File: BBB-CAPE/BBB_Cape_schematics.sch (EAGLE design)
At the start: 63 parts, among them IC1 EEPROM-I2CSMD

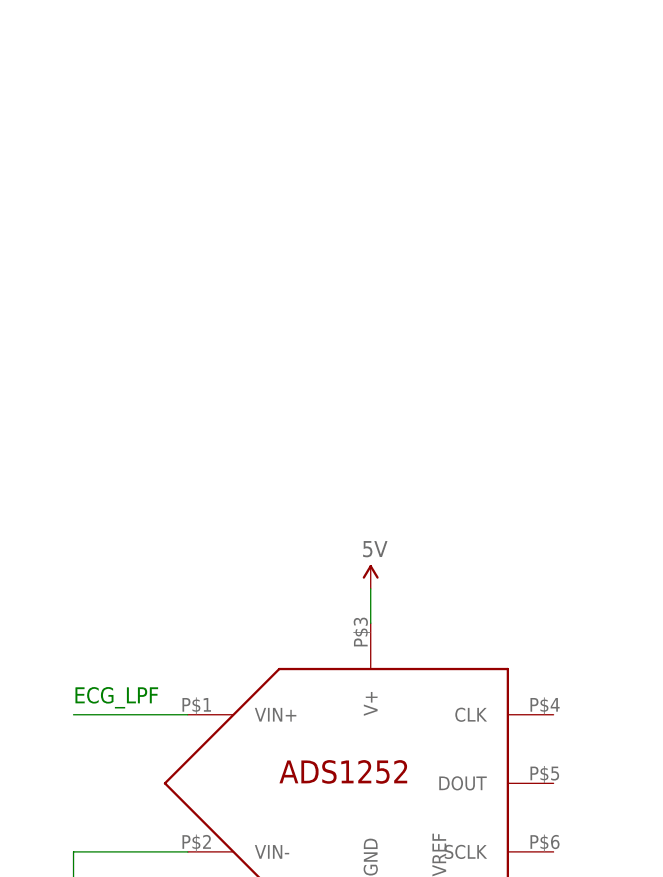
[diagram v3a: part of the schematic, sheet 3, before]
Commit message: Add Clock ATS16ASM-1 to BBB_Cape_schematics.sch
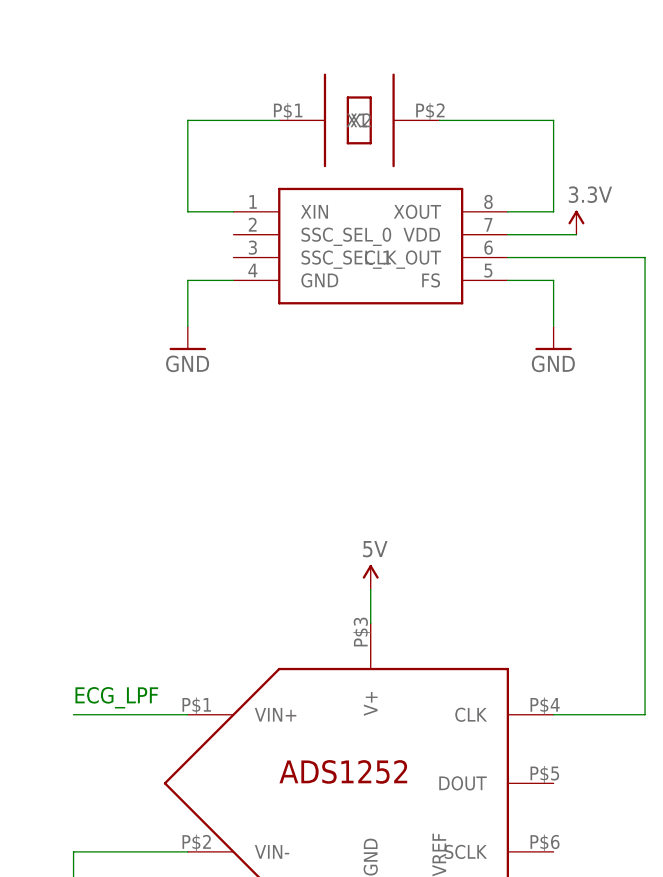
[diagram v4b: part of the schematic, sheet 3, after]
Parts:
- added U$10: CDCS502, Components:CDCS502
- added U$23: ATS16ASM-1, Components:ATS16ASM-1
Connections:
- new net N$27: U$10.XIN, U$23.X1
- new net N$28: U$10.XOUT, U$23.X2
- new net N$29: U$10.CLK_OUT, U$19.CLK
- net 3.3V: now also U$10.VDD
- net GND: now also U$10.FS, U$10.GND

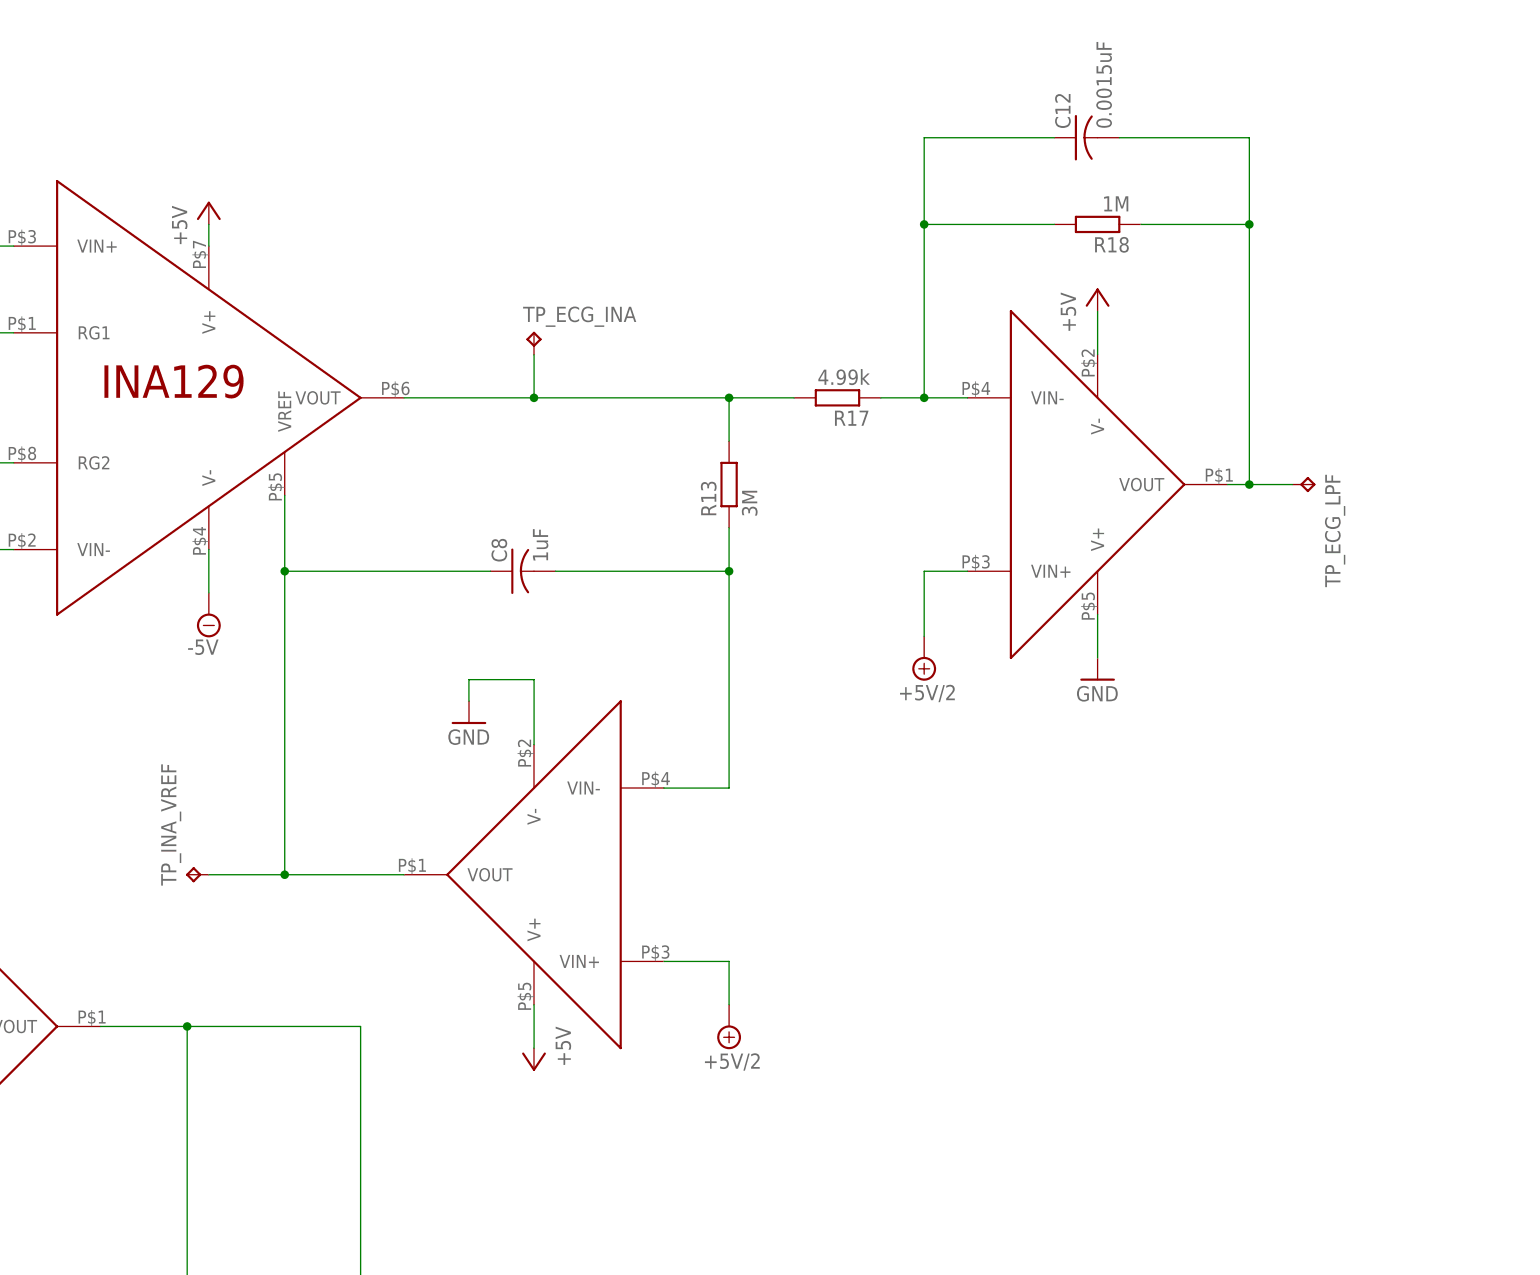
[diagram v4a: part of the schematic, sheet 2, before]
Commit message: Add Resistors to INA129 HPF and LMP2021 LPF for selecting different cut-off frequency; Add DIP Switch  in BBB_Cape_schematics.sch
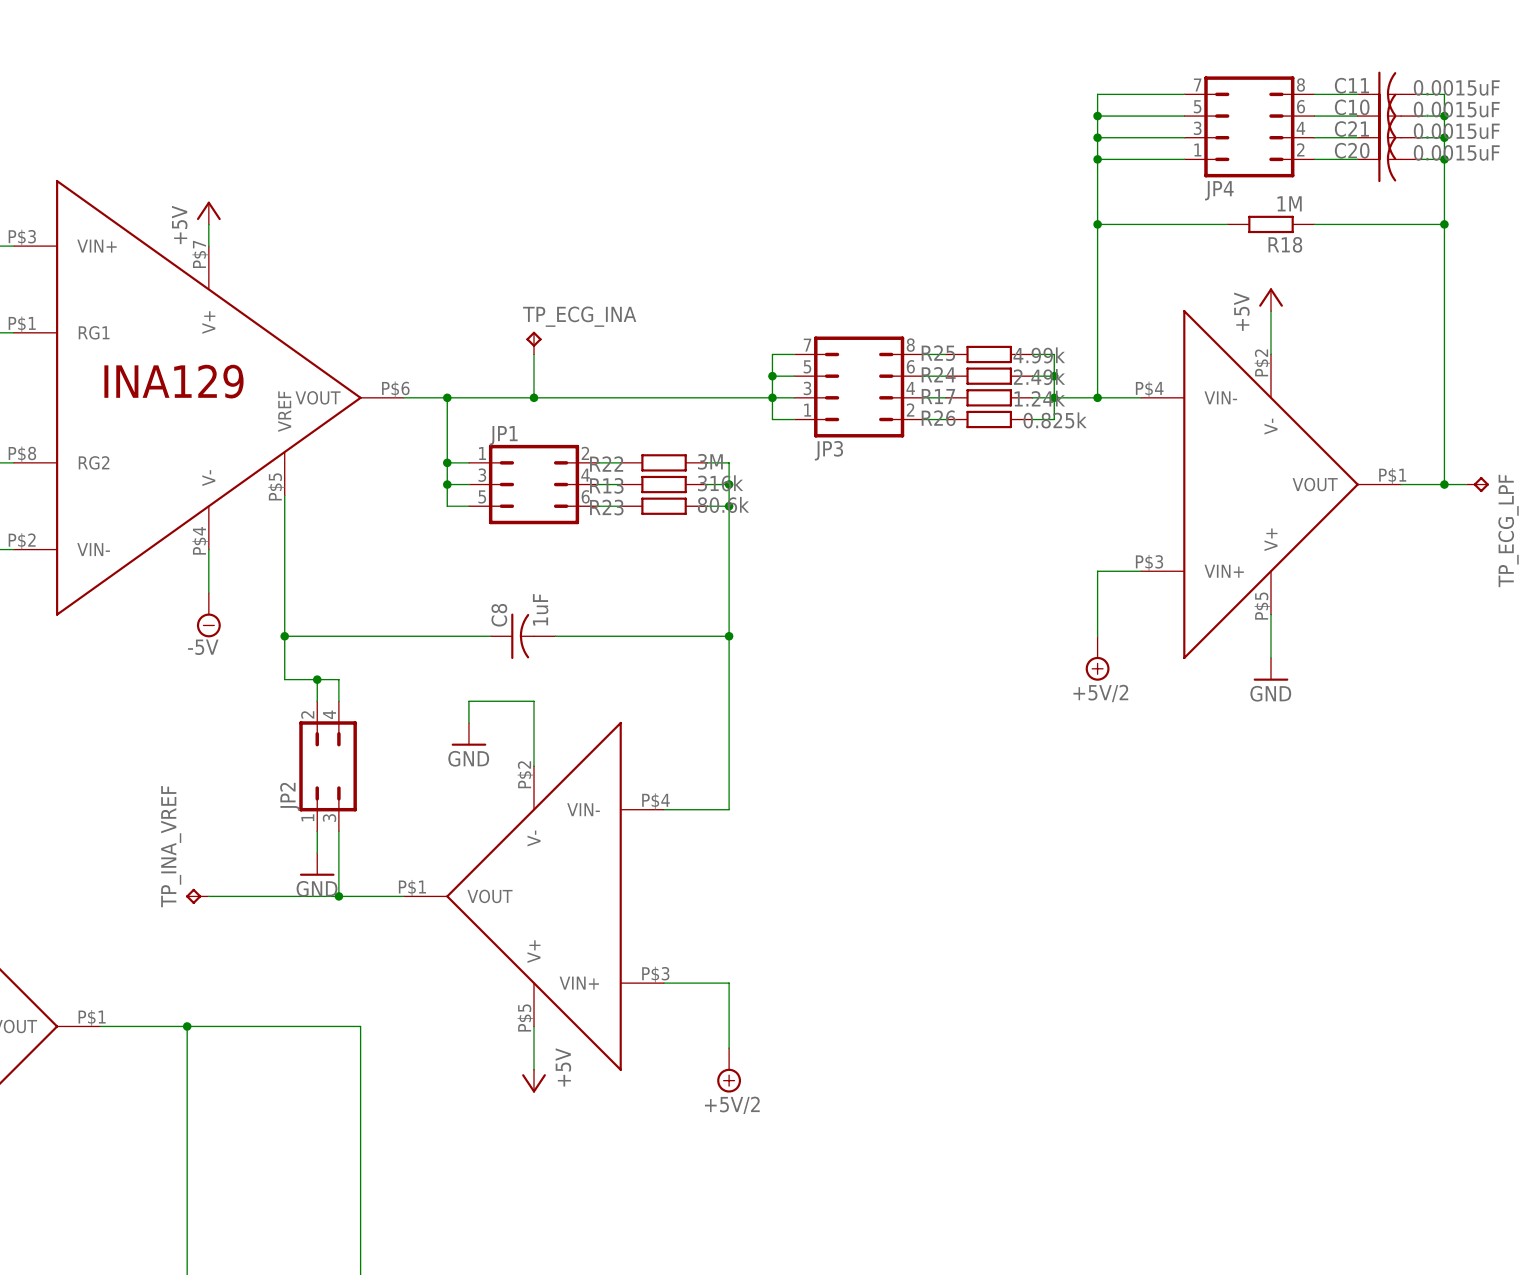
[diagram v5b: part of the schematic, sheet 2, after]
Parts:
- removed C12: 0.0015uF, rcl:C-USC1206
- removed S1: SW_DIP-2P, logic-supply:SW_DIP-2P
- added C10, C11, C20, C21: 0.0015uF, rcl:C-USC1206
- added JP1: (no value), jumper:JP3Q
- added JP2: (no value), jumper:JP2Q
- added JP3, JP4: (no value), jumper:JP4Q
- added R20, R21: 10k, resistor:R-EU_M1206
- added R22: 3M, resistor:R-EU_M1206
- added R23: 80.6k, resistor:R-EU_M1206
- added R24: 2.49k, resistor:R-EU_M1206
- added R25: 4.99k, resistor:R-EU_M1206
- added R26: 0.825k, resistor:R-EU_M1206
- added S2, SW1, SW2: 219-02, switch-dil:219-02
- R13: value 3M -> 316k
- R17: value 4.99k -> 1.24k
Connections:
- new net ADC_DOUT: BB1P9.GPIO0_4, U$19.DOUT
- new net ADC_SCLK: BB1P9.SERIAL2_RX/GGPIO0_2, U$19.SCLK
- new net N$30: R21.2, S2.4, U$10.SSC_SEL_0
- new net N$31: R20.2, S2.3, U$10.SSC_SEL_1
- new net N$32: JP1.2, R22.1
- new net N$33: JP1.4, R13.1
- new net N$34: JP1.6, R23.1
- new net N$35: JP2.3, TP_INA_VREF.TP, U$9.VOUT
- new net N$36: BB1P9.3.3V@1, SW1.4
- new net N$37: JP3.8, R25.2
- new net N$38: JP3.6, R24.2
- new net N$39: JP3.4, R17.2
- new net N$40: JP3.2, R26.2
- new net N$41: C11.1, JP4.8
- new net N$42: C10.1, JP4.6
- new net N$43: C21.1, JP4.4
- new net N$44: C20.1, JP4.2
- new net N$45: BB1P9.5V_RAW@1, SW1.3
- net 3.3V: now also S2.1, S2.2, SW1.1; no longer BB1P9.3.3V@1
- net 5V: now also SW1.2; no longer BB1P9.5V_RAW@1
- net GND: now also JP2.1, R20.1, R21.1, SW2.1, SW2.2; no longer S1.1A, S1.2A
- net N$10: now also JP2.2, JP2.4; no longer TP_INA_VREF.TP, U$9.VOUT
- net N$11: now also JP1.1, JP1.3, JP1.5, JP3.1, JP3.3, JP3.5, JP3.7; no longer R13.2, R17.2
- net N$12: now also R13.2, R22.2, R23.2; no longer R13.1
- net N$13: now also SW2.4; no longer S1.1B
- net N$14: now also SW2.3; no longer S1.2B
- net N$18: now also JP4.1, JP4.3, JP4.5, JP4.7, R24.1, R25.1, R26.1; no longer C12.1
- net N$20: now also C10.2, C11.2, C20.2, C21.2; no longer C12.2
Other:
- note added: "ADC_DOUT"
- note added: "ADC_SCLK"
- moved on the sheet: C8, R13, R17, R18, TP_ECG_LPF, TP_INA_VREF
